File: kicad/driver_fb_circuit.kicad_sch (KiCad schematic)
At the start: 51 parts, among them Q1 IRFZ44N, Q2 IRFZ44N, Q3 IRFZ44N, Q4 IRFZ44N, Q5 IRFZ44N, Q6 IRFZ44N, U1 IR2104, U2 IR2104, U3 IR2104, U4 INA180A2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

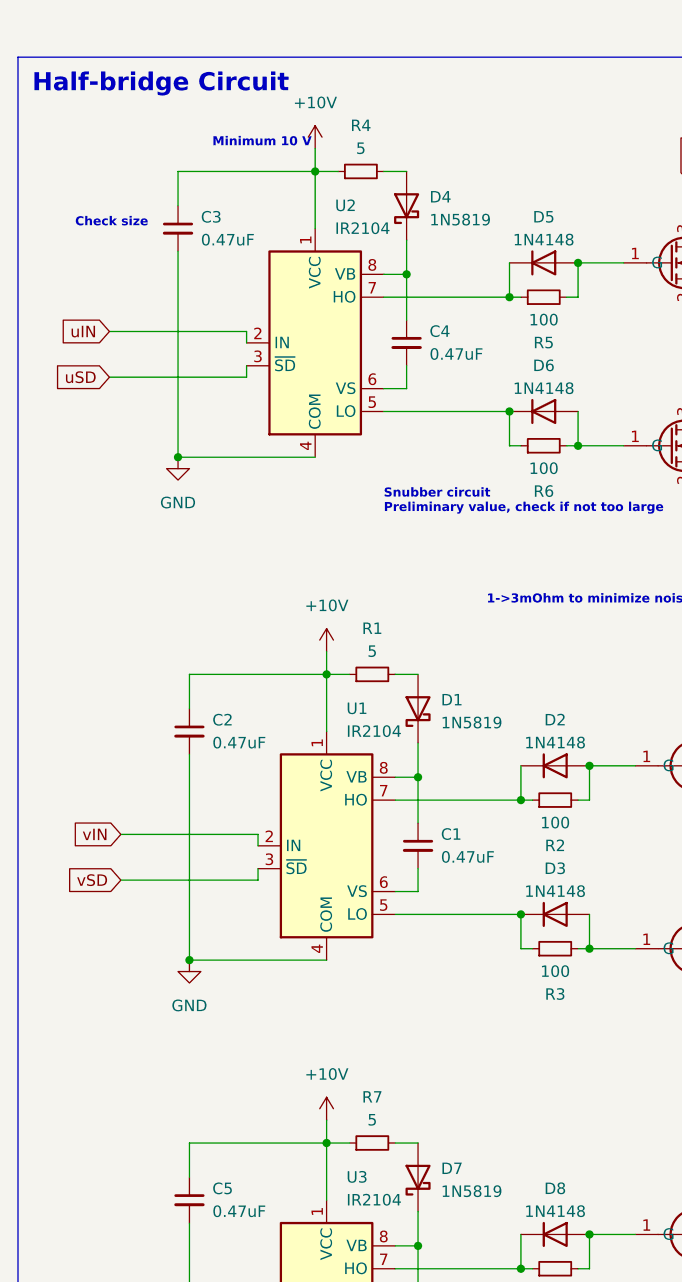
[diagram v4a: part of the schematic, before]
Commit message: [kicad] Added linear regulator, buck converter, priority-based power-input MUX | TODO: Add complete buck converter circuit, add resistive divider to linear regulator [simulations] Added correct buck converter simulation
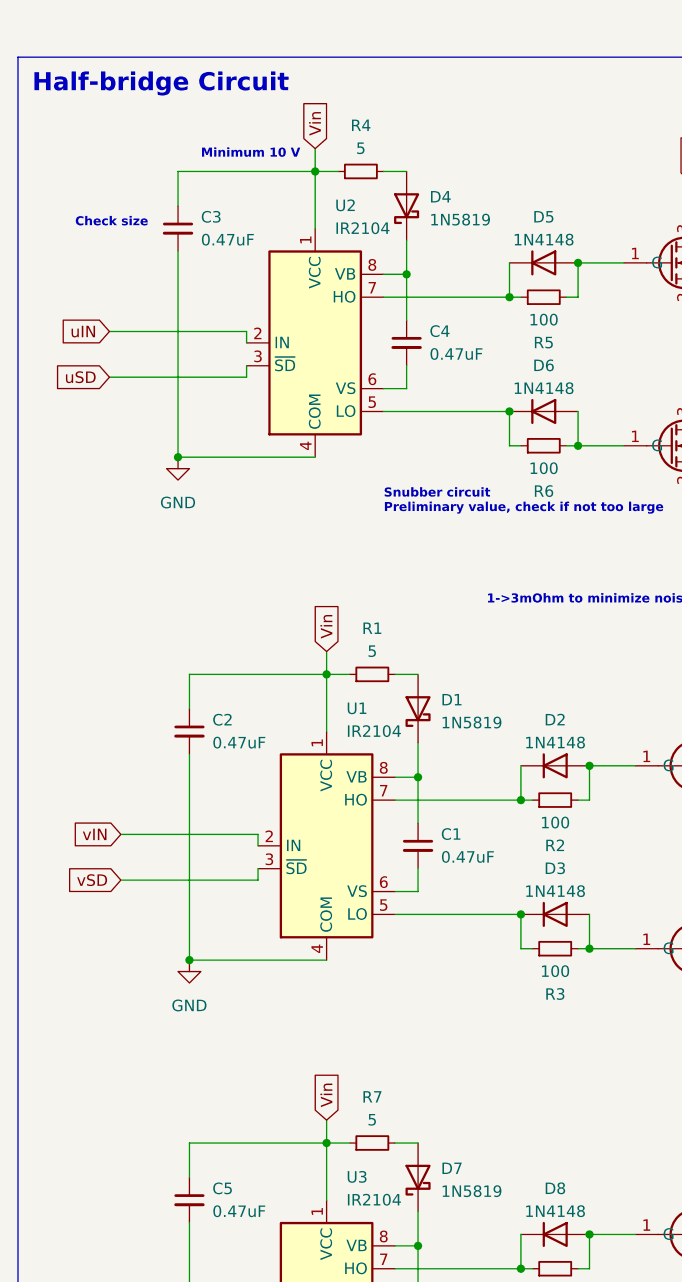
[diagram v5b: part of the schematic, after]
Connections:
- net +10V is gone; now on net Vin: C2.1, C3.1, C5.1, R1.1, R4.1, R7.1, U1.1 (VCC), U2.1 (VCC), U3.1 (VCC)
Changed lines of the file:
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@@
     (effects (font (size 1 1) bold) (justify left bottom))
   )
-  (text "Minimum 10 V" (at 41.91 27.94 0)
+  (text "Minimum 10 V" (at 40.64 29.21 0)
     (effects (font (size 1 1) bold) (justify left bottom))
   )
@@
     )
   )
+  (global_label "Vin" (shape input) (at 54.61 135.89 90) (fields_autoplaced)
+    (effects (font (size 1.27 1.27)) (justify left))
+    (property "Intersheetrefs" "${INTERSHEET_REFS}" (at 54.61 130.0624 90)
+      (effects (font (size 1.27 1.27)) (justify left) hide)
+    )
+  )
   (global_label "uPHASE" (shape input) (at 107.95 50.8 0) (fields_autoplaced)
     (effects (font (size 1.27 1.27)) (justify left))
     (property "Intersheetrefs" "${INTERSHEET_REFS}" (at 118.1318 50.8 0)
+      (effects (font (size 1.27 1.27)) (justify left) hide)
+    )
+  )
+  (global_label "Vin" (shape input) (at 54.61 83.82 90) (fields_autoplaced)
+    (effects (font (size 1.27 1.27)) (justify left))
+    (property "Intersheetrefs" "${INTERSHEET_REFS}" (at 54.61 77.9924 90)
       (effects (font (size 1.27 1.27)) (justify left) hide)
     )
@@
     )
   )
+  (global_label "Vin" (shape input) (at 53.34 27.94 90) (fields_autoplaced)
+    (effects (font (size 1.27 1.27)) (justify left))
+    (property "Intersheetrefs" "${INTERSHEET_REFS}" (at 53.34 22.1124 90)
+      (effects (font (size 1.27 1.27)) (justify left) hide)
+    )
+  )
   (global_label "vCURRENT" (shape input) (at 128.27 128.27 0) (fields_autoplaced)
     (effects (font (size 1.27 1.27)) (justify left))
@@
         (path "/91e2f46a-700b-4d7a-a06a-22469f63223f/7f7e17e0-7d73-4fbb-9112-49949fae378a"
           (reference "#PWR07") (unit 1)
-        )
-      )
-    )
-  )
-  (symbol (lib_id "power:+10V") (at 54.61 83.82 0) (unit 1)
-    (in_bom yes) (on_board yes) (dnp no) (fields_autoplaced)
-    (property "Reference" "#PWR046" (at 54.61 87.63 0)
-      (effects (font (size 1.27 1.27)) hide)
-    )
-    (property "Value" "+10V" (at 54.61 78.74 0)
-      (effects (font (size 1.27 1.27)))
-    )
-    (property "Footprint" "" (at 54.61 83.82 0)
-      (effects (font (size 1.27 1.27)) hide)
-    )
-    (property "Datasheet" "" (at 54.61 83.82 0)
-      (effects (font (size 1.27 1.27)) hide)
-    )
-    (pin "1")
-    (instances
-      (project "bldc_project"
-        (path "/91e2f46a-700b-4d7a-a06a-22469f63223f/7f7e17e0-7d73-4fbb-9112-49949fae378a"
-          (reference "#PWR046") (unit 1)
         )
       )
@@
     )
   )
-  (symbol (lib_id "power:+10V") (at 53.34 27.94 0) (unit 1)
-    (in_bom yes) (on_board yes) (dnp no) (fields_autoplaced)
-    (property "Reference" "#PWR042" (at 53.34 31.75 0)
-      (effects (font (size 1.27 1.27)) hide)
-    )
-    (property "Value" "+10V" (at 53.34 22.86 0)
-      (effects (font (size 1.27 1.27)))
-    )
-    (property "Footprint" "" (at 53.34 27.94 0)
-      (effects (font (size 1.27 1.27)) hide)
-    )
-    (property "Datasheet" "" (at 53.34 27.94 0)
-      (effects (font (size 1.27 1.27)) hide)
-    )
-    (pin "1")
-    (instances
-      (project "bldc_project"
-        (path "/91e2f46a-700b-4d7a-a06a-22469f63223f/7f7e17e0-7d73-4fbb-9112-49949fae378a"
-          (reference "#PWR042") (unit 1)
-        )
-      )
-    )
-  )
   (symbol (lib_id "Driver_FET:IR2104") (at 54.61 157.48 0) (unit 1)
     (in_bom yes) (on_board yes) (dnp no) (fields_autoplaced)
@@
         )
       )
-    )
-  )
-  (symbol (lib_id "power:+10V") (at 54.61 135.89 0) (unit 1)
-    (in_bom yes) (on_board yes) (dnp no) (fields_autoplaced)
-    (property "Reference" "#PWR047" (at 54.61 139.7 0)
-      (effects (font (size 1.27 1.27)) hide)
-    )
-    (property "Value" "+10V" (at 54.61 130.81 0)
-      (effects (font (size 1.27 1.27)))
-    )
-    (property "Footprint" "" (at 54.61 135.89 0)
-      (effects (font (size 1.27 1.27)) hide)
-    )
-    (property "Datasheet" "" (at 54.61 135.89 0)
-      (effects (font (size 1.27 1.27)) hide)
-    )
-    (pin "1")
-    (instances
-      (project "bldc_project"
-        (path "/91e2f46a-700b-4d7a-a06a-22469f63223f/7f7e17e0-7d73-4fbb-9112-49949fae378a"
-          (reference "#PWR047") (unit 1)
-        )
-      )
